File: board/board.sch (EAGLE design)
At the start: 17 parts

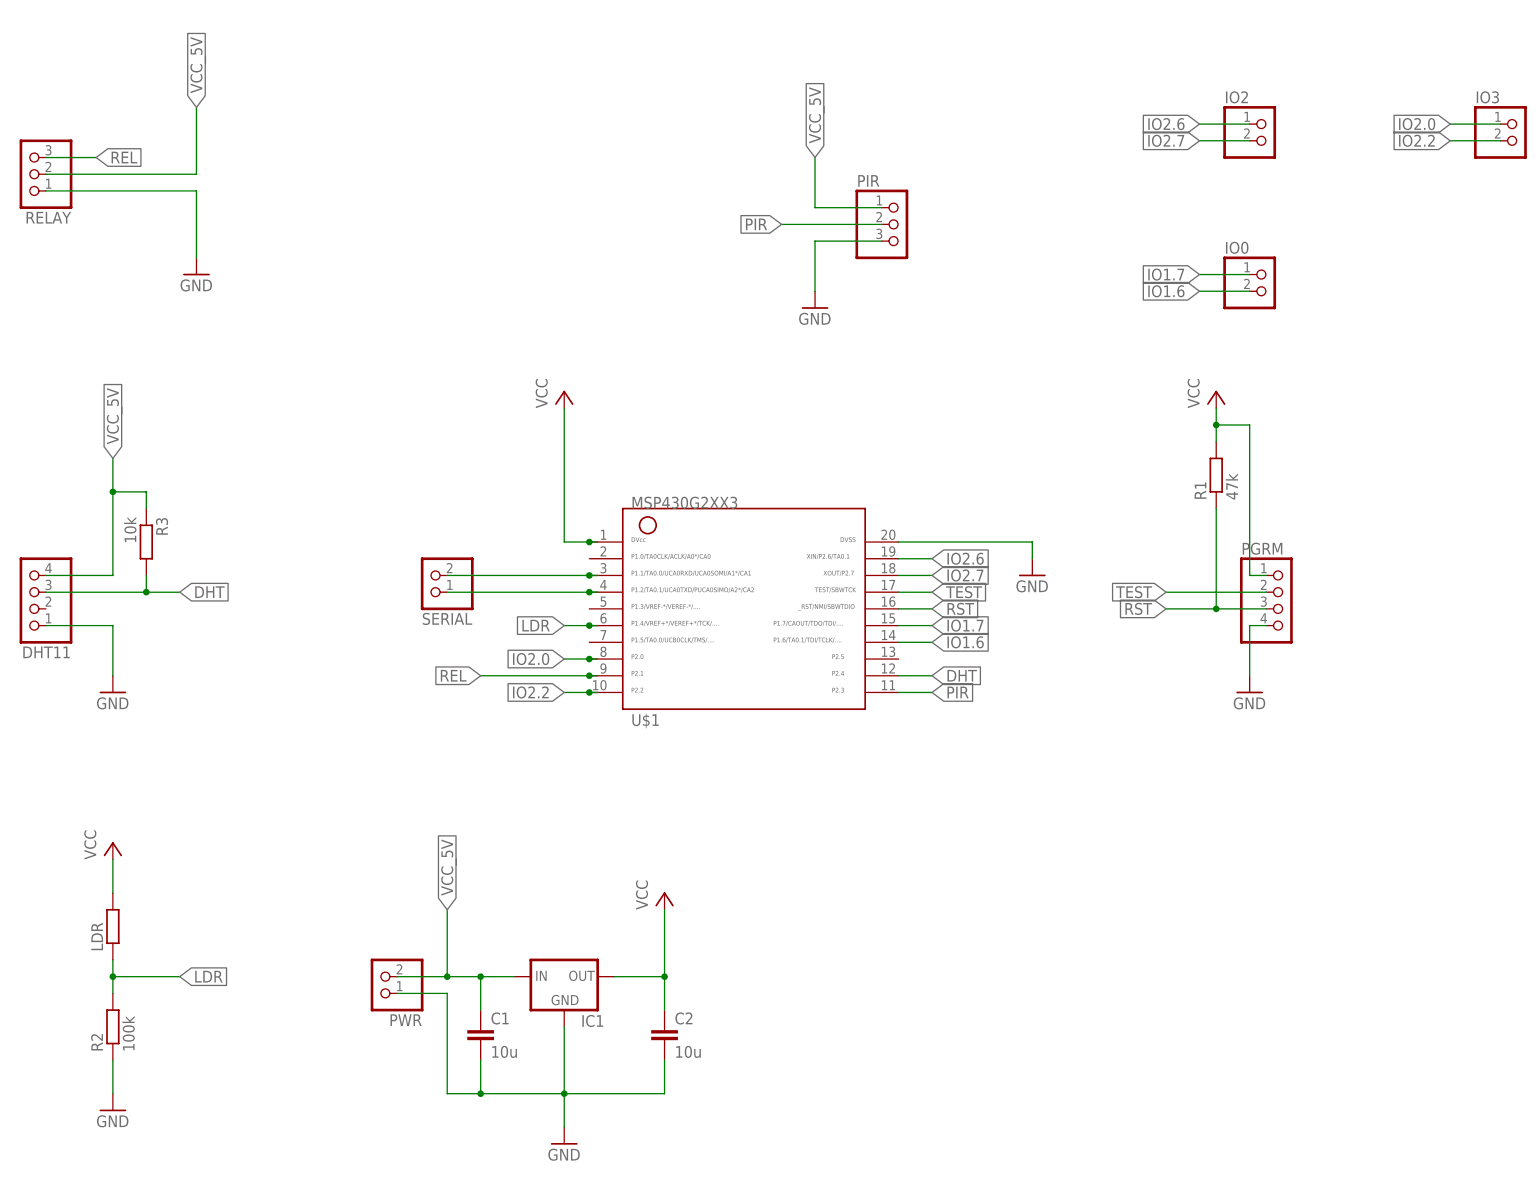
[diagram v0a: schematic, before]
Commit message: fixed some space issues of the v0.1 board
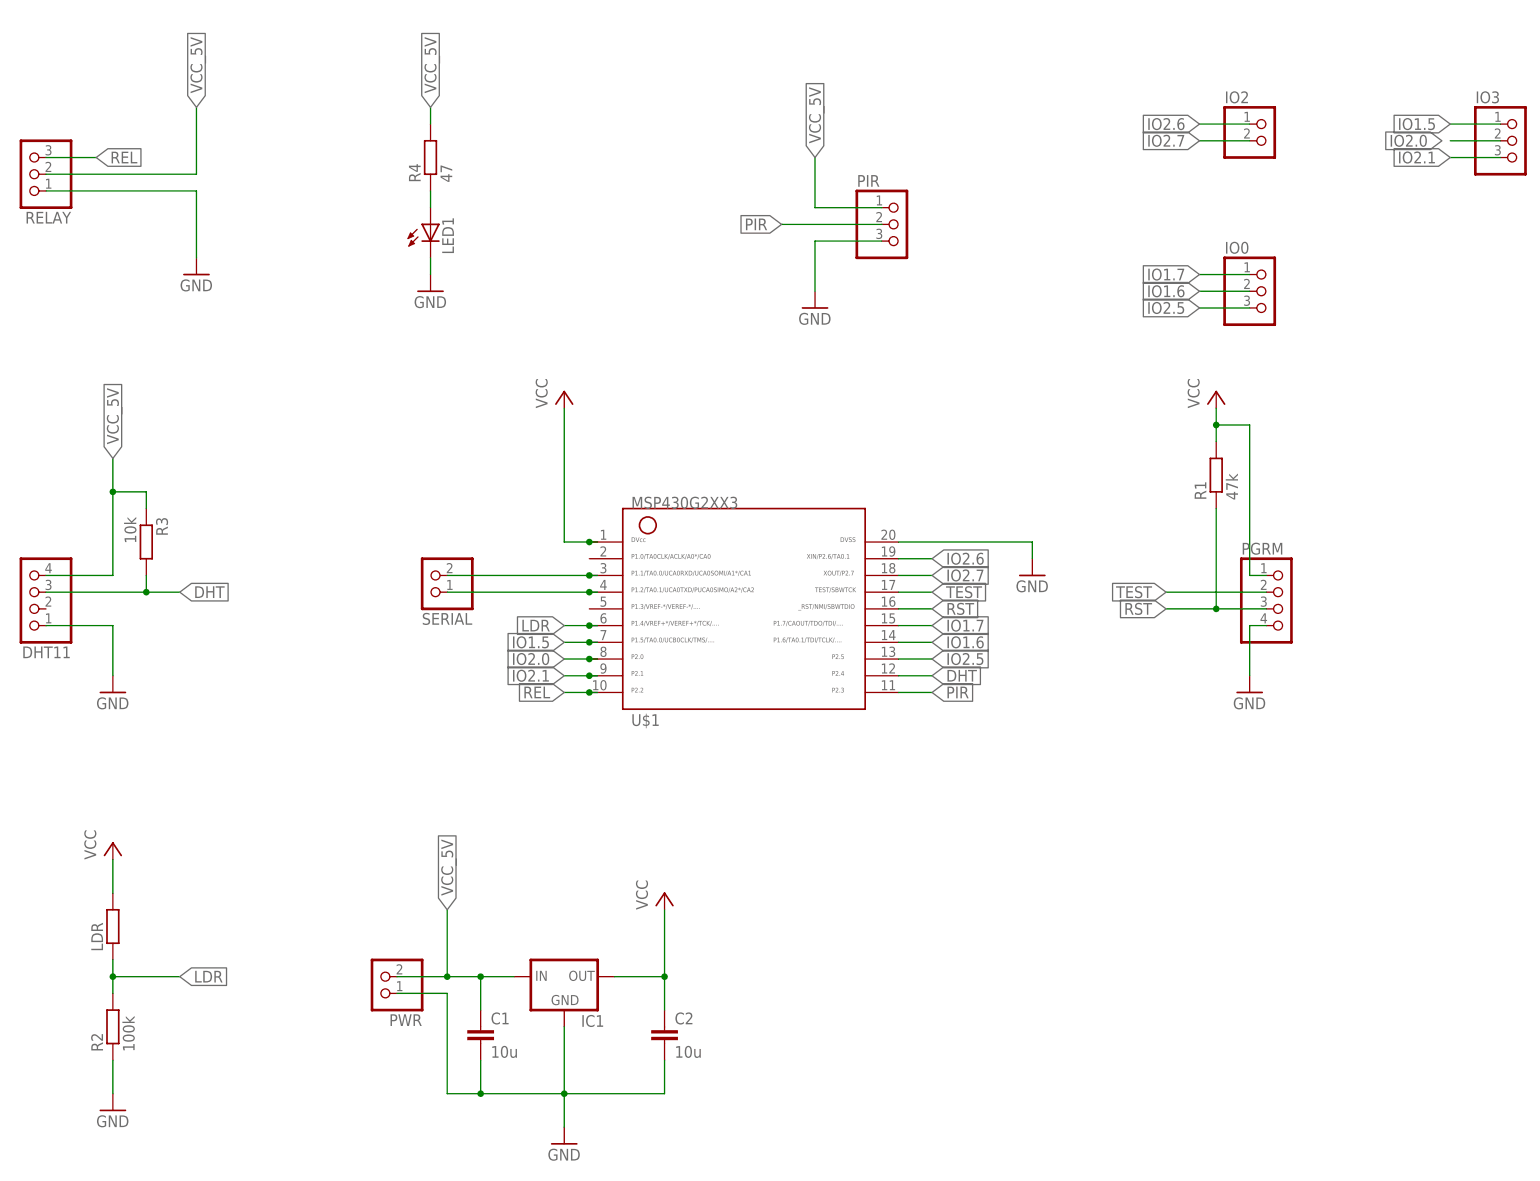
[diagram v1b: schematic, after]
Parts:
- added LED1: (no value), led:LED3MM
- added R4: 47, rcl:R-EU_0207/10
- IO0, IO3: device pinhead:PINHD-1X2 -> pinhead:PINHD-1X3
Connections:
- removed net IO2.2: IO3.2, U$1.10
- new net IO1.5: IO3.1, U$1.7
- new net IO2.1: IO3.3, U$1.9
- new net IO2.5: IO0.3, U$1.13
- new net N$1: LED1.A, R4.1
- net GND: now also LED1.C
- net IO2.0: now also IO3.2; no longer IO3.1
- net REL: now also U$1.10; no longer U$1.9
- net VCC_5V: now also R4.2
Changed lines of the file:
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@@
 <setting verticaltext="up"/>
 </settings>
-<grid distance="0.1" unitdist="inch" unit="inch" style="lines" multiple="1" display="no" altdistance="0.01" altunitdist="inch" altunit="inch"/>
+<grid distance="0.1" unitdist="inch" unit="inch" style="dots" multiple="1" display="yes" altdistance="0.01" altunitdist="inch" altunit="inch"/>
 <layers>
 <layer number="1" name="Top" color="4" fill="1" visible="no" active="no"/>
@@
 <part name="C2" library="rcl" deviceset="C-EU" device="025-025X050" value="10u"/>
 <part name="IO2" library="pinhead" deviceset="PINHD-1X2" device=""/>
-<part name="IO0" library="pinhead" deviceset="PINHD-1X2" device=""/>
-<part name="IO3" library="pinhead" deviceset="PINHD-1X2" device=""/>
+<part name="IO0" library="pinhead" deviceset="PINHD-1X3" device=""/>
+<part name="IO3" library="pinhead" deviceset="PINHD-1X3" device=""/>
 <part name="PIR" library="pinhead" deviceset="PINHD-1X3" device=""/>
 <part name="GND7" library="supply1" deviceset="GND" device=""/>
+<part name="LED1" library="led" deviceset="LED" device="3MM"/>
+<part name="GND8" library="supply1" deviceset="GND" device=""/>
+<part name="R4" library="rcl" deviceset="R-EU_" device="0207/10" value="47"/>
 </parts>
 <sheets>
@@
 <instance part="C2" gate="G$1" x="114.3" y="22.86"/>
 <instance part="IO2" gate="G$1" x="205.74" y="157.48"/>
-<instance part="IO0" gate="G$1" x="205.74" y="134.62"/>
-<instance part="IO3" gate="G$1" x="243.84" y="157.48"/>
+<instance part="IO0" gate="A" x="205.74" y="134.62"/>
+<instance part="IO3" gate="A" x="243.84" y="157.48"/>
 <instance part="PIR" gate="A" x="149.86" y="144.78"/>
 <instance part="GND7" gate="1" x="137.16" y="132.08"/>
+<instance part="LED1" gate="G$1" x="78.74" y="144.78"/>
+<instance part="GND8" gate="1" x="78.74" y="134.62"/>
+<instance part="R4" gate="G$1" x="78.74" y="154.94" rot="R90"/>
 </instances>
 <busses>
@@
 <pinref part="GND7" gate="1" pin="GND"/>
 </segment>
+<segment>
+<pinref part="LED1" gate="G$1" pin="C"/>
+<pinref part="GND8" gate="1" pin="GND"/>
+<wire x1="78.74" y1="139.7" x2="78.74" y2="137.16" width="0.1524" layer="91"/>
+</segment>
 </net>
 <net name="VCC" class="0">
@@
 <label x="137.16" y="154.94" size="1.778" layer="95" rot="R90" xref="yes"/>
 </segment>
+<segment>
+<pinref part="R4" gate="G$1" pin="2"/>
+<wire x1="78.74" y1="160.02" x2="78.74" y2="162.56" width="0.1524" layer="91"/>
+<label x="78.74" y="162.56" size="1.778" layer="95" rot="R90" xref="yes"/>
+</segment>
 </net>
 <net name="DHT" class="0">
@@
 <net name="REL" class="0">
 <segment>
-<wire x1="104.14" y1="76.2" x2="102.87" y2="76.2" width="0.1524" layer="91"/>
-<label x="86.36" y="76.2" size="1.778" layer="95" rot="R180" xref="yes"/>
-<pinref part="U$1" gate="G$1" pin="9"/>
-<wire x1="102.87" y1="76.2" x2="86.36" y2="76.2" width="0.1524" layer="91"/>
-<junction x="102.87" y="76.2"/>
-</segment>
-<segment>
 <pinref part="RELAY" gate="A" pin="3"/>
 <wire x1="20.32" y1="154.94" x2="27.94" y2="154.94" width="0.1524" layer="91"/>
 <label x="27.94" y="154.94" size="1.778" layer="95" xref="yes"/>
 </segment>
+<segment>
+<wire x1="104.14" y1="73.66" x2="102.87" y2="73.66" width="0.1524" layer="91"/>
+<pinref part="U$1" gate="G$1" pin="10"/>
+<wire x1="102.87" y1="73.66" x2="99.06" y2="73.66" width="0.1524" layer="91"/>
+<junction x="102.87" y="73.66"/>
+<label x="99.06" y="73.66" size="1.778" layer="95" rot="R180" xref="yes"/>
+</segment>
 </net>
 <net name="TEST" class="0">
@@
 </segment>
 <segment>
-<pinref part="IO0" gate="G$1" pin="1"/>
+<pinref part="IO0" gate="A" pin="1"/>
 <wire x1="203.2" y1="137.16" x2="195.58" y2="137.16" width="0.1524" layer="91"/>
 <label x="195.58" y="137.16" size="1.778" layer="95" rot="R180" xref="yes"/>
@@
 </segment>
 <segment>
-<pinref part="IO0" gate="G$1" pin="2"/>
+<pinref part="IO0" gate="A" pin="2"/>
 <wire x1="203.2" y1="134.62" x2="195.58" y2="134.62" width="0.1524" layer="91"/>
 <label x="195.58" y="134.62" size="1.778" layer="95" rot="R180" xref="yes"/>
@@
 </segment>
 <segment>
-<pinref part="IO3" gate="G$1" pin="1"/>
-<wire x1="241.3" y1="160.02" x2="233.68" y2="160.02" width="0.1524" layer="91"/>
-<label x="233.68" y="160.02" size="1.778" layer="95" rot="R180" xref="yes"/>
-</segment>
-</net>
-<net name="IO2.2" class="0">
-<segment>
-<wire x1="104.14" y1="73.66" x2="102.87" y2="73.66" width="0.1524" layer="91"/>
-<label x="99.06" y="73.66" size="1.778" layer="95" rot="R180" xref="yes"/>
-<pinref part="U$1" gate="G$1" pin="10"/>
-<junction x="102.87" y="73.66"/>
-<wire x1="102.87" y1="73.66" x2="99.06" y2="73.66" width="0.1524" layer="91"/>
-</segment>
-<segment>
-<pinref part="IO3" gate="G$1" pin="2"/>
+<pinref part="IO3" gate="A" pin="2"/>
 <wire x1="241.3" y1="157.48" x2="233.68" y2="157.48" width="0.1524" layer="91"/>
-<label x="233.68" y="157.48" size="1.778" layer="95" rot="R180" xref="yes"/>
+<label x="232.41" y="157.48" size="1.778" layer="95" rot="R180" xref="yes"/>
 </segment>
 </net>
@@
 </segment>
 </net>
+<net name="IO1.5" class="0">
+<segment>
+<wire x1="104.14" y1="81.28" x2="102.87" y2="81.28" width="0.1524" layer="91"/>
+<pinref part="U$1" gate="G$1" pin="7"/>
+<junction x="102.87" y="81.28"/>
+<wire x1="102.87" y1="81.28" x2="99.06" y2="81.28" width="0.1524" layer="91"/>
+<label x="99.06" y="81.28" size="1.778" layer="95" rot="R180" xref="yes"/>
+</segment>
+<segment>
+<pinref part="IO3" gate="A" pin="1"/>
+<wire x1="241.3" y1="160.02" x2="233.68" y2="160.02" width="0.1524" layer="91"/>
+<label x="233.68" y="160.02" size="1.778" layer="95" rot="R180" xref="yes"/>
+</segment>
+</net>
+<net name="IO2.1" class="0">
+<segment>
+<wire x1="104.14" y1="76.2" x2="102.87" y2="76.2" width="0.1524" layer="91"/>
+<pinref part="U$1" gate="G$1" pin="9"/>
+<wire x1="102.87" y1="76.2" x2="99.06" y2="76.2" width="0.1524" layer="91"/>
+<junction x="102.87" y="76.2"/>
+<label x="99.06" y="76.2" size="1.778" layer="95" rot="R180" xref="yes"/>
+</segment>
+<segment>
+<pinref part="IO3" gate="A" pin="3"/>
+<wire x1="241.3" y1="154.94" x2="233.68" y2="154.94" width="0.1524" layer="91"/>
+<label x="233.68" y="154.94" size="1.778" layer="95" rot="R180" xref="yes"/>
+</segment>
+</net>
+<net name="IO2.5" class="0">
+<segment>
+<pinref part="U$1" gate="G$1" pin="13"/>
+<wire x1="149.86" y1="78.74" x2="154.94" y2="78.74" width="0.1524" layer="91"/>
+<label x="154.94" y="78.74" size="1.778" layer="95" xref="yes"/>
+</segment>
+<segment>
+<pinref part="IO0" gate="A" pin="3"/>
+<wire x1="203.2" y1="132.08" x2="195.58" y2="132.08" width="0.1524" layer="91"/>
+<label x="195.58" y="132.08" size="1.778" layer="95" rot="R180" xref="yes"/>
+</segment>
+</net>
+<net name="N$1" class="0">
+<segment>
+<pinref part="R4" gate="G$1" pin="1"/>
+<pinref part="LED1" gate="G$1" pin="A"/>
+<wire x1="78.74" y1="149.86" x2="78.74" y2="147.32" width="0.1524" layer="91"/>
+</segment>
+</net>

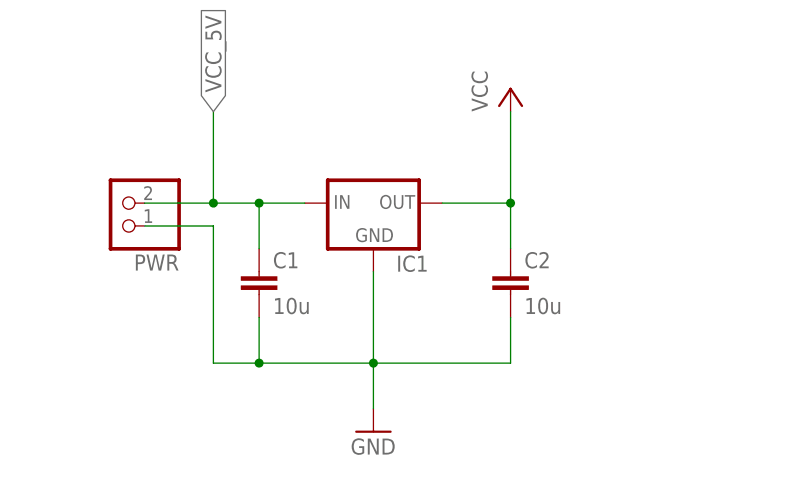
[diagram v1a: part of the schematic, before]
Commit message: finished the v02 board
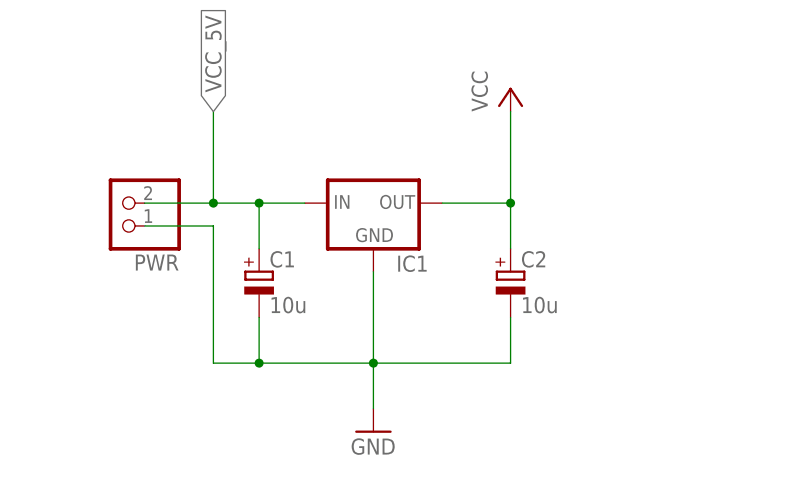
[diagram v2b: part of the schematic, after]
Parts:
- C1, C2: device rcl:C-EU025-025X050 -> rcl:CPOL-EUE2.5-5
- LDR: device rcl:R-EU_0204/2V -> rcl:R-EU_0207/5V
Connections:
- net GND: now also C1.-, C2.-; no longer C1.2, C2.2
- net VCC: now also C2.+; no longer C2.1
- net VCC_5V: now also C1.+; no longer C1.1
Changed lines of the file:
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@@
 <part name="P+3" library="supply1" deviceset="VCC" device=""/>
 <part name="GND2" library="supply1" deviceset="GND" device=""/>
-<part name="LDR" library="rcl" deviceset="R-EU_" device="0204/2V"/>
+<part name="LDR" library="rcl" deviceset="R-EU_" device="0207/5V"/>
 <part name="IC1" library="adafruit" deviceset="MCP1700" device="TRI"/>
 <part name="P+4" library="supply1" deviceset="VCC" device=""/>
@@
 <part name="PGRM" library="pinhead" deviceset="PINHD-1X4" device=""/>
 <part name="GND6" library="supply1" deviceset="GND" device=""/>
-<part name="C1" library="rcl" deviceset="C-EU" device="025-025X050" value="10u"/>
-<part name="C2" library="rcl" deviceset="C-EU" device="025-025X050" value="10u"/>
+<part name="C1" library="rcl" deviceset="CPOL-EU" device="E2.5-5" value="10u"/>
+<part name="C2" library="rcl" deviceset="CPOL-EU" device="E2.5-5" value="10u"/>
 <part name="IO2" library="pinhead" deviceset="PINHD-1X2" device=""/>
 <part name="IO0" library="pinhead" deviceset="PINHD-1X3" device=""/>
@@
 <wire x1="81.28" y1="12.7" x2="86.36" y2="12.7" width="0.1524" layer="91"/>
 <junction x="99.06" y="12.7"/>
-<pinref part="C2" gate="G$1" pin="2"/>
+<pinref part="C2" gate="G$1" pin="-"/>
 <wire x1="86.36" y1="12.7" x2="99.06" y2="12.7" width="0.1524" layer="91"/>
 <wire x1="114.3" y1="17.78" x2="114.3" y2="12.7" width="0.1524" layer="91"/>
 <wire x1="114.3" y1="12.7" x2="99.06" y2="12.7" width="0.1524" layer="91"/>
-<pinref part="C1" gate="G$1" pin="2"/>
+<pinref part="C1" gate="G$1" pin="-"/>
 <wire x1="86.36" y1="17.78" x2="86.36" y2="12.7" width="0.1524" layer="91"/>
 <junction x="86.36" y="12.7"/>
@@
 <wire x1="106.68" y1="30.48" x2="114.3" y2="30.48" width="0.1524" layer="91"/>
 <wire x1="114.3" y1="30.48" x2="114.3" y2="40.64" width="0.1524" layer="91"/>
-<pinref part="C2" gate="G$1" pin="1"/>
+<pinref part="C2" gate="G$1" pin="+"/>
 <wire x1="114.3" y1="30.48" x2="114.3" y2="25.4" width="0.1524" layer="91"/>
 <junction x="114.3" y="30.48"/>
@@
 <label x="81.28" y="40.64" size="1.778" layer="95" rot="R90" xref="yes"/>
 <junction x="81.28" y="30.48"/>
-<pinref part="C1" gate="G$1" pin="1"/>
+<pinref part="C1" gate="G$1" pin="+"/>
 <wire x1="86.36" y1="30.48" x2="86.36" y2="25.4" width="0.1524" layer="91"/>
 <junction x="86.36" y="30.48"/>

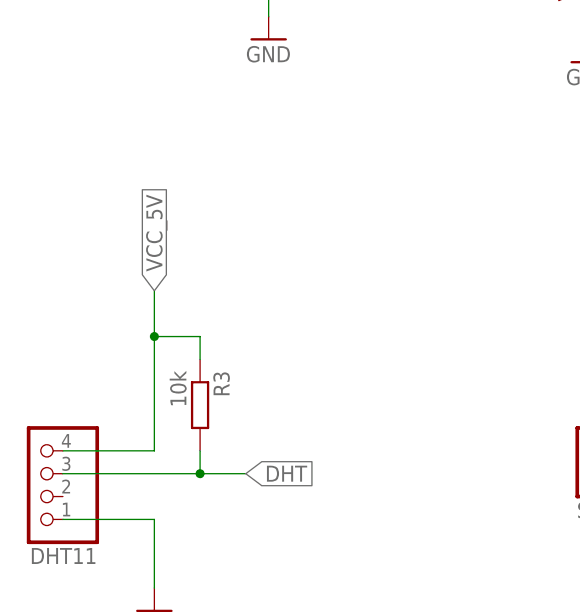
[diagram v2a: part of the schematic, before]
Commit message: updated the board and firmware to a new revision / pin mapping is now correct and installing a PIR sensor is a lot easier
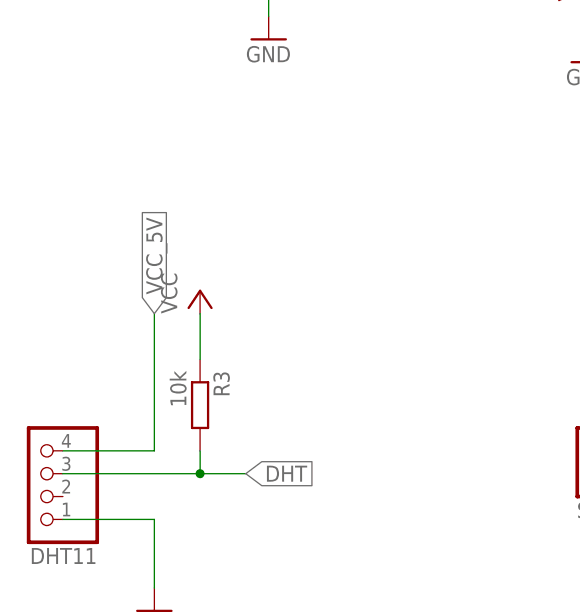
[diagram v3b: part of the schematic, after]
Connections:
- net VCC: now also R3.1
- net VCC_5V: no longer R3.1
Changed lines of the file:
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@@
 <setting verticaltext="up"/>
 </settings>
-<grid distance="0.1" unitdist="inch" unit="inch" style="dots" multiple="1" display="yes" altdistance="0.01" altunitdist="inch" altunit="inch"/>
+<grid distance="0.1" unitdist="inch" unit="inch" style="lines" multiple="1" display="no" altdistance="0.01" altunitdist="inch" altunit="inch"/>
 <layers>
 <layer number="1" name="Top" color="4" fill="1" visible="no" active="no"/>
@@
 <part name="GND8" library="supply1" deviceset="GND" device=""/>
 <part name="R4" library="rcl" deviceset="R-EU_" device="0207/10" value="47"/>
+<part name="P+5" library="supply1" deviceset="VCC" device=""/>
 </parts>
 <sheets>
@@
 <instance part="GND8" gate="1" x="78.74" y="134.62"/>
 <instance part="R4" gate="G$1" x="78.74" y="154.94" rot="R90"/>
+<instance part="P+5" gate="VCC" x="35.56" y="109.22"/>
 </instances>
 <busses>
@@
 <junction x="114.3" y="30.48"/>
 </segment>
+<segment>
+<pinref part="R3" gate="G$1" pin="1"/>
+<wire x1="35.56" y1="101.6" x2="35.56" y2="106.68" width="0.1524" layer="91"/>
+<pinref part="P+5" gate="VCC" pin="VCC"/>
+</segment>
 </net>
 <net name="N$2" class="0">
@@
 </segment>
 <segment>
-<pinref part="DHT11" gate="A" pin="4"/>
-<wire x1="20.32" y1="91.44" x2="30.48" y2="91.44" width="0.1524" layer="91"/>
-<wire x1="30.48" y1="91.44" x2="30.48" y2="104.14" width="0.1524" layer="91"/>
-<label x="30.48" y="109.22" size="1.778" layer="95" rot="R90" xref="yes"/>
-<pinref part="R3" gate="G$1" pin="1"/>
-<wire x1="30.48" y1="104.14" x2="30.48" y2="109.22" width="0.1524" layer="91"/>
-<wire x1="35.56" y1="101.6" x2="35.56" y2="104.14" width="0.1524" layer="91"/>
-<wire x1="35.56" y1="104.14" x2="30.48" y2="104.14" width="0.1524" layer="91"/>
-<junction x="30.48" y="104.14"/>
-</segment>
-<segment>
 <pinref part="RELAY" gate="A" pin="2"/>
 <wire x1="20.32" y1="152.4" x2="43.18" y2="152.4" width="0.1524" layer="91"/>
@@
 <label x="78.74" y="162.56" size="1.778" layer="95" rot="R90" xref="yes"/>
 </segment>
-</net>
+<segment>
+<pinref part="DHT11" gate="A" pin="4"/>
+<wire x1="20.32" y1="91.44" x2="30.48" y2="91.44" width="0.1524" layer="91"/>
+<wire x1="30.48" y1="91.44" x2="30.48" y2="106.68" width="0.1524" layer="91"/>
+<label x="30.48" y="106.68" size="1.778" layer="95" rot="R90" xref="yes"/>
+</segment>
+</net>
